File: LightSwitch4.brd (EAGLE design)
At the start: 40 x 44 mm, 9 parts, among them SW1 SWITCH-SPST-ILLUMINATED, SW2 SWITCH-SPST-ILLUMINATED, SW3 SWITCH-SPST-ILLUMINATED, SW4 SWITCH-SPST-ILLUMINATED

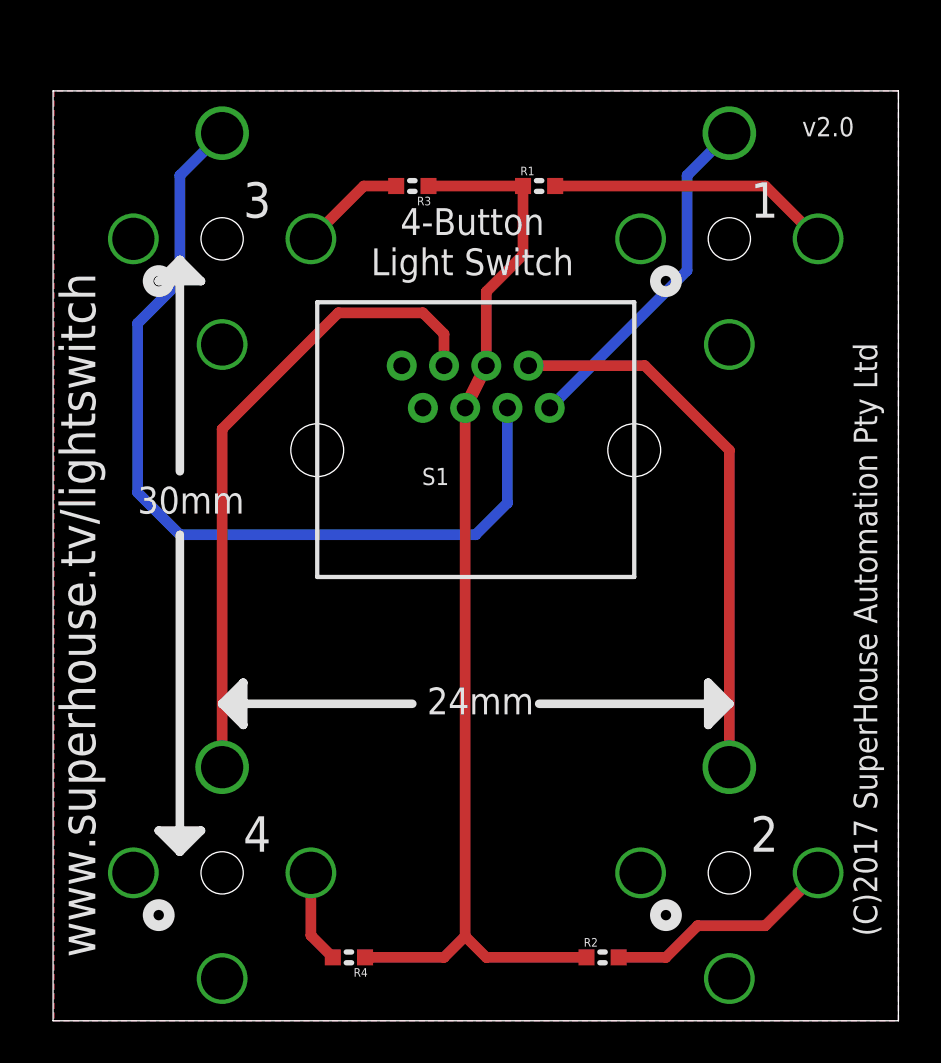
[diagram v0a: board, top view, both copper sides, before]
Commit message: Changed button footprint to slotted version for v2.1 release
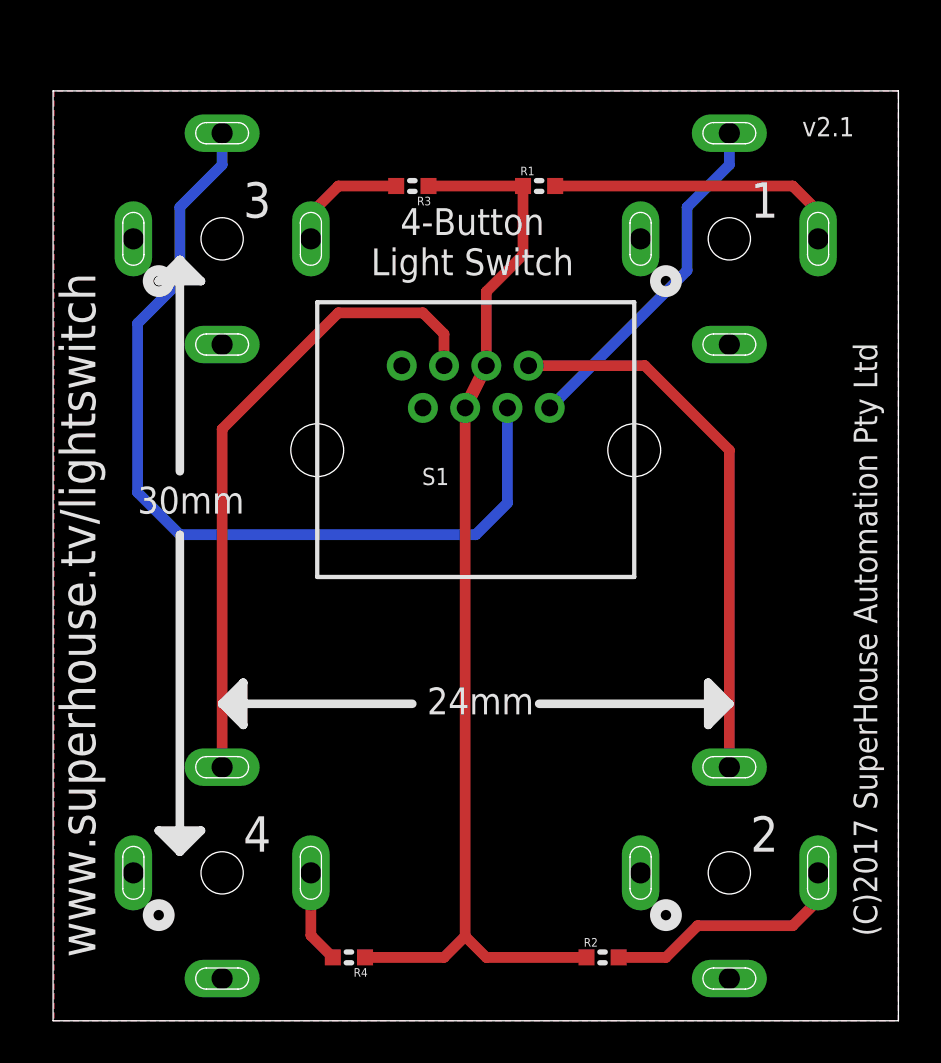
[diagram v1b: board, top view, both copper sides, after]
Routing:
- net N$1: track 11.1 -> 11.9 mm
- net N$6: track 13.5 -> 14.2 mm
- net N$7: track 5.07 -> 5.78 mm
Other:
- board text added: "v2.1"
- board text removed: "v2.0"
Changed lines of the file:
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@@
 <?xml version="1.0" encoding="utf-8"?>
 <!DOCTYPE eagle SYSTEM "eagle.dtd">
-<eagle version="8.3.2">
+<eagle version="8.7.0">
 <drawing>
 <settings>
-<setting alwaysvectorfont="yes"/>
+<setting alwaysvectorfont="no"/>
 <setting keepoldvectorfont="yes"/>
 <setting verticaltext="up"/>
@@
 <layer number="60" name="p_dimension" color="6" fill="0" visible="no" active="no"/>
 <layer number="61" name="pt_docu" color="7" fill="0" visible="no" active="no"/>
+<layer number="88" name="SimResults" color="9" fill="1" visible="no" active="no"/>
+<layer number="89" name="SimProbes" color="9" fill="1" visible="no" active="no"/>
 <layer number="90" name="Modules" color="7" fill="1" visible="no" active="no"/>
 <layer number="91" name="Nets" color="2" fill="1" visible="no" active="no"/>
@@
 <wire x1="40" y1="44" x2="40" y2="0" width="0" layer="20"/>
 <text x="39" y="4" size="1.1176" layer="21" font="vector" ratio="15" rot="R90">(C)2017 SuperHouse Automation Pty Ltd</text>
-<text x="35.4452" y="41.8486" size="0.9144" layer="21" font="vector" ratio="15">v2.0</text>
+<text x="35.4452" y="41.8486" size="0.9144" layer="21" font="vector" ratio="15">v2.1</text>
 <text x="19.8412" y="36.8646" size="1.27" layer="21" font="vector" ratio="15" align="center">4-Button
 Light Switch</text>
-<text x="2" y="3" size="1.6764" layer="21" ratio="15" rot="R90">www.superhouse.tv/lightswitch</text>
-<text x="33" y="38" size="1.6764" layer="21" ratio="15">1</text>
-<text x="33" y="8" size="1.6764" layer="21" ratio="15">2</text>
-<text x="9" y="38" size="1.6764" layer="21" ratio="15">3</text>
-<text x="9" y="8" size="1.6764" layer="21" ratio="15">4</text>
-<text x="17.7" y="14.5" size="1.27" layer="21" ratio="15">24mm</text>
+<text x="2" y="3" size="1.6764" layer="21" font="vector" ratio="15" rot="R90">www.superhouse.tv/lightswitch</text>
+<text x="33" y="38" size="1.6764" layer="21" font="vector" ratio="15">1</text>
+<text x="33" y="8" size="1.6764" layer="21" font="vector" ratio="15">2</text>
+<text x="9" y="38" size="1.6764" layer="21" font="vector" ratio="15">3</text>
+<text x="9" y="8" size="1.6764" layer="21" font="vector" ratio="15">4</text>
+<text x="17.7" y="14.5" size="1.27" layer="21" font="vector" ratio="15">24mm</text>
 <wire x1="17" y1="15" x2="8" y2="15" width="0.4064" layer="21"/>
 <wire x1="8" y1="15" x2="9" y2="16" width="0.4064" layer="21"/>
@@
 <wire x1="31" y1="16" x2="31" y2="14" width="0.4064" layer="21"/>
 <wire x1="31" y1="14" x2="32" y2="15" width="0.4064" layer="21"/>
-<text x="4" y="24" size="1.27" layer="21" ratio="15">30mm</text>
+<text x="4" y="24" size="1.27" layer="21" font="vector" ratio="15">30mm</text>
 <wire x1="6" y1="26" x2="6" y2="36" width="0.4064" layer="21"/>
 <wire x1="6" y1="36" x2="7" y2="35" width="0.4064" layer="21"/>
@@
 <param name="dpMaxLengthDifference" value="10mm"/>
 <param name="dpGapFactor" value="2.5"/>
-<param name="checkGrid" value="0"/>
 <param name="checkAngle" value="0"/>
 <param name="checkFont" value="1"/>
 <param name="checkRestrict" value="1"/>
+<param name="checkStop" value="0"/>
+<param name="checkValues" value="0"/>
 <param name="useDiameter" value="13"/>
 <param name="maxErrors" value="50"/>
@@
 <contactref element="SW1" pad="3"/>
 <wire x1="23.5" y1="29" x2="30" y2="35.5" width="0.508" layer="16"/>
-<wire x1="30" y1="40" x2="32" y2="42" width="0.508" layer="16"/>
-<wire x1="30" y1="35.5" x2="30" y2="40" width="0.508" layer="16"/>
+<wire x1="30" y1="35.5" x2="30" y2="38.5" width="0.508" layer="16"/>
+<wire x1="30" y1="38.5" x2="32" y2="40.5" width="0.508" layer="16"/>
+<wire x1="32" y1="40.5" x2="32" y2="42" width="0.508" layer="16"/>
 </signal>
 <signal name="N$5">
@@
 <wire x1="4" y1="25" x2="4" y2="33" width="0.508" layer="16"/>
 <wire x1="4" y1="33" x2="6" y2="35" width="0.508" layer="16"/>
-<wire x1="6" y1="35" x2="6" y2="40" width="0.508" layer="16"/>
-<wire x1="6" y1="40" x2="8" y2="42" width="0.508" layer="16"/>
+<wire x1="6" y1="35" x2="6" y2="38.5" width="0.508" layer="16"/>
+<wire x1="6" y1="38.5" x2="8" y2="40.5" width="0.508" layer="16"/>
+<wire x1="8" y1="40.5" x2="8" y2="42" width="0.508" layer="16"/>
 </signal>
 <signal name="N$3">
@@
 <contactref element="R2" pad="2"/>
 <wire x1="29" y1="3" x2="30.5" y2="4.5" width="0.508" layer="1"/>
-<wire x1="33.7" y1="4.5" x2="36.2" y2="7" width="0.508" layer="1"/>
 <wire x1="26.762" y1="3" x2="29" y2="3" width="0.508" layer="1"/>
-<wire x1="30.5" y1="4.5" x2="33.7" y2="4.5" width="0.508" layer="1"/>
+<wire x1="35" y1="4.5" x2="36.2" y2="5.7" width="0.508" layer="1"/>
+<wire x1="36.2" y1="5.7" x2="36.2" y2="7" width="0.508" layer="1"/>
+<wire x1="30.5" y1="4.5" x2="35" y2="4.5" width="0.508" layer="1"/>
 </signal>
 <signal name="N$6">
 <contactref element="SW1" pad="2"/>
 <contactref element="R1" pad="2"/>
-<wire x1="23.762" y1="39.5" x2="33.7" y2="39.5" width="0.508" layer="1"/>
-<wire x1="33.7" y1="39.5" x2="36.2" y2="37" width="0.508" layer="1"/>
+<wire x1="35" y1="39.5" x2="36.2" y2="38.3" width="0.508" layer="1"/>
+<wire x1="36.2" y1="38.3" x2="36.2" y2="37" width="0.508" layer="1"/>
+<wire x1="23.762" y1="39.5" x2="35" y2="39.5" width="0.508" layer="1"/>
 </signal>
 <signal name="N$7">
 <contactref element="SW3" pad="2"/>
 <contactref element="R3" pad="2"/>
-<wire x1="16.238" y1="39.5" x2="14.7" y2="39.5" width="0.508" layer="1"/>
-<wire x1="14.7" y1="39.5" x2="12.2" y2="37" width="0.508" layer="1"/>
+<wire x1="16.238" y1="39.5" x2="13.5" y2="39.5" width="0.508" layer="1"/>
+<wire x1="13.5" y1="39.5" x2="12.2" y2="38.2" width="0.508" layer="1"/>
+<wire x1="12.2" y1="38.2" x2="12.2" y2="37" width="0.508" layer="1"/>
 </signal>
 <signal name="N$8">
@@
 </signal>
 </signals>
-<errors>
-</errors>
 </board>
 </drawing>

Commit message: Updated RJ45 footprint for v2.2
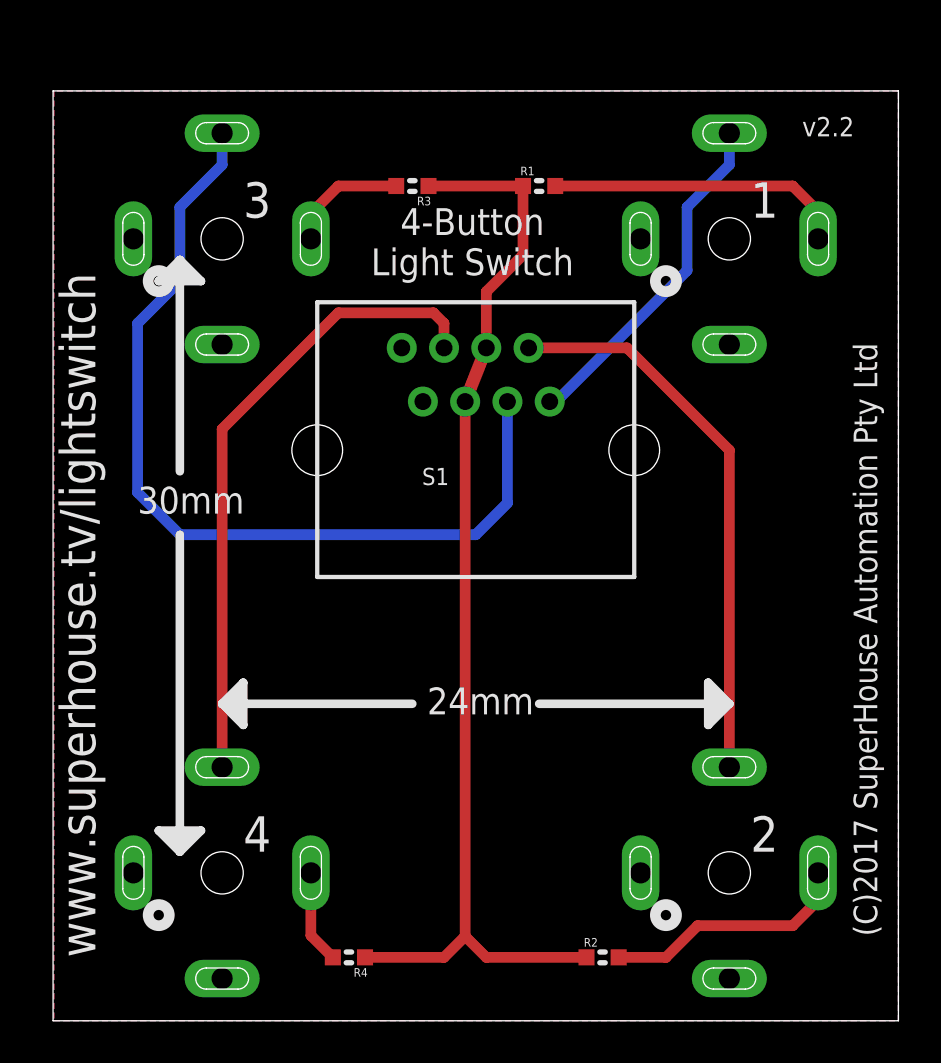
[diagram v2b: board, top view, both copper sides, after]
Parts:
- R1, R2, R3, R4: value 3K3 -> 4K7
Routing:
- net N$3: track 30.7 -> 30.1 mm
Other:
- board text added: "v2.2"
- board text removed: "v2.1"
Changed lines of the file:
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@@
 <wire x1="40" y1="44" x2="40" y2="0" width="0" layer="20"/>
 <text x="39" y="4" size="1.1176" layer="21" font="vector" ratio="15" rot="R90">(C)2017 SuperHouse Automation Pty Ltd</text>
-<text x="35.4452" y="41.8486" size="0.9144" layer="21" font="vector" ratio="15">v2.1</text>
+<text x="35.4452" y="41.8486" size="0.9144" layer="21" font="vector" ratio="15">v2.2</text>
 <text x="19.8412" y="36.8646" size="1.27" layer="21" font="vector" ratio="15" align="center">4-Button
 Light Switch</text>
@@
 <element name="SW3" library="freetronics-jon" package="SWITCH-SPST-ILLUMINATED" value="SWITCH-SPST-ILLUMINATED" x="8" y="37" rot="MR0"/>
 <element name="SW4" library="freetronics-jon" package="SWITCH-SPST-ILLUMINATED" value="SWITCH-SPST-ILLUMINATED" x="8" y="7" rot="MR0"/>
-<element name="R1" library="freetronics-jon" package="0603" value="3K3" x="23" y="39.5"/>
-<element name="R2" library="freetronics-jon" package="0603" value="3K3" x="26" y="3"/>
-<element name="R3" library="freetronics-jon" package="0603" value="3K3" x="17" y="39.5" rot="R180"/>
-<element name="R4" library="freetronics-jon" package="0603" value="3K3" x="14" y="3" rot="R180"/>
+<element name="R1" library="freetronics-jon" package="0603" value="4K7" x="23" y="39.5"/>
+<element name="R2" library="freetronics-jon" package="0603" value="4K7" x="26" y="3"/>
+<element name="R3" library="freetronics-jon" package="0603" value="4K7" x="17" y="39.5" rot="R180"/>
+<element name="R4" library="freetronics-jon" package="0603" value="4K7" x="14" y="3" rot="R180"/>
 </elements>
 <signals>
@@
 <contactref element="S1" pad="5"/>
 <contactref element="S1" pad="4"/>
-<wire x1="19.5" y1="29" x2="20.5" y2="31" width="0.6096" layer="1"/>
+<wire x1="19.5" y1="29.3" x2="20.5" y2="31.84" width="0.6096" layer="1"/>
 <contactref element="R4" pad="1"/>
 <contactref element="R3" pad="1"/>
@@
 <contactref element="R1" pad="1"/>
 <wire x1="22.238" y1="39.5" x2="17.762" y2="39.5" width="0.508" layer="1"/>
-<wire x1="20.5" y1="31" x2="20.5" y2="34.5" width="0.508" layer="1"/>
+<wire x1="20.5" y1="31.84" x2="20.5" y2="34.5" width="0.508" layer="1"/>
 <wire x1="22.238" y1="36.238" x2="22.238" y2="39.5" width="0.508" layer="1"/>
 <wire x1="20.5" y1="34.5" x2="22.238" y2="36.238" width="0.508" layer="1"/>
 <wire x1="19.5" y1="4" x2="20.5" y2="3" width="0.508" layer="1"/>
 <wire x1="20.5" y1="3" x2="25.238" y2="3" width="0.508" layer="1"/>
-<wire x1="19.5" y1="29" x2="19.5" y2="4" width="0.508" layer="1"/>
+<wire x1="19.5" y1="29.3" x2="19.5" y2="4" width="0.508" layer="1"/>
 <wire x1="14.762" y1="3" x2="18.5" y2="3" width="0.508" layer="1"/>
 <wire x1="18.5" y1="3" x2="19.5" y2="4" width="0.508" layer="1"/>
@@
 <contactref element="S1" pad="1"/>
 <contactref element="SW1" pad="3"/>
-<wire x1="23.5" y1="29" x2="30" y2="35.5" width="0.508" layer="16"/>
-<wire x1="30" y1="35.5" x2="30" y2="38.5" width="0.508" layer="16"/>
+<wire x1="30" y1="38.5" x2="30" y2="35.5" width="0.508" layer="16"/>
 <wire x1="30" y1="38.5" x2="32" y2="40.5" width="0.508" layer="16"/>
 <wire x1="32" y1="40.5" x2="32" y2="42" width="0.508" layer="16"/>
+<wire x1="30" y1="35.5" x2="23.8" y2="29.3" width="0.508" layer="16"/>
+<wire x1="23.8" y1="29.3" x2="23.5" y2="29.3" width="0.508" layer="16"/>
 </signal>
 <signal name="N$5">
@@
 <contactref element="SW2" pad="3"/>
 <wire x1="32" y1="12" x2="32" y2="27" width="0.508" layer="1"/>
-<wire x1="32" y1="27" x2="28" y2="31" width="0.508" layer="1"/>
-<wire x1="28" y1="31" x2="22.5" y2="31" width="0.508" layer="1"/>
+<wire x1="27.16" y1="31.84" x2="22.5" y2="31.84" width="0.508" layer="1"/>
+<wire x1="32" y1="27" x2="27.16" y2="31.84" width="0.508" layer="1"/>
 </signal>
 <signal name="N$2">
 <contactref element="S1" pad="3"/>
 <contactref element="SW3" pad="3"/>
-<wire x1="21.5" y1="29" x2="21.5" y2="24.5" width="0.508" layer="16"/>
+<wire x1="21.5" y1="29.3" x2="21.5" y2="24.5" width="0.508" layer="16"/>
 <wire x1="21.5" y1="24.5" x2="20" y2="23" width="0.508" layer="16"/>
 <wire x1="20" y1="23" x2="6" y2="23" width="0.508" layer="16"/>
@@
 <wire x1="8" y1="12" x2="8" y2="28" width="0.508" layer="1"/>
 <wire x1="8" y1="28" x2="13.5" y2="33.5" width="0.508" layer="1"/>
-<wire x1="13.5" y1="33.5" x2="17.5" y2="33.5" width="0.508" layer="1"/>
-<wire x1="17.5" y1="33.5" x2="18.5" y2="32.5" width="0.508" layer="1"/>
-<wire x1="18.5" y1="32.5" x2="18.5" y2="31" width="0.508" layer="1"/>
+<wire x1="18" y1="33.5" x2="18.5" y2="33" width="0.508" layer="1"/>
+<wire x1="18.5" y1="33" x2="18.5" y2="31.84" width="0.508" layer="1"/>
+<wire x1="13.5" y1="33.5" x2="18" y2="33.5" width="0.508" layer="1"/>
 </signal>
 <signal name="N$1">

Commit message: Release v2.2
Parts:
- S1: value RJ45 -> RJ45JC
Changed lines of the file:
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@@
 <?xml version="1.0" encoding="utf-8"?>
 <!DOCTYPE eagle SYSTEM "eagle.dtd">
-<eagle version="8.7.0">
+<eagle version="9.2.1">
 <drawing>
 <settings>
@@
 <param name="checkStop" value="0"/>
 <param name="checkValues" value="0"/>
+<param name="checkNames" value="1"/>
+<param name="checkWireStubs" value="1"/>
+<param name="checkPolygonWidth" value="0"/>
 <param name="useDiameter" value="13"/>
 <param name="maxErrors" value="50"/>
@@
 </autorouter>
 <elements>
-<element name="S1" library="freetronics-jon" package="RJ45" value="RJ45" x="20" y="27"/>
-<element name="SW1" library="freetronics-jon" package="SWITCH-SPST-ILLUMINATED" value="SWITCH-SPST-ILLUMINATED" x="32" y="37" rot="MR0"/>
-<element name="SW2" library="freetronics-jon" package="SWITCH-SPST-ILLUMINATED" value="SWITCH-SPST-ILLUMINATED" x="32" y="7" rot="MR0"/>
-<element name="SW3" library="freetronics-jon" package="SWITCH-SPST-ILLUMINATED" value="SWITCH-SPST-ILLUMINATED" x="8" y="37" rot="MR0"/>
-<element name="SW4" library="freetronics-jon" package="SWITCH-SPST-ILLUMINATED" value="SWITCH-SPST-ILLUMINATED" x="8" y="7" rot="MR0"/>
-<element name="R1" library="freetronics-jon" package="0603" value="4K7" x="23" y="39.5"/>
-<element name="R2" library="freetronics-jon" package="0603" value="4K7" x="26" y="3"/>
-<element name="R3" library="freetronics-jon" package="0603" value="4K7" x="17" y="39.5" rot="R180"/>
-<element name="R4" library="freetronics-jon" package="0603" value="4K7" x="14" y="3" rot="R180"/>
+<element name="S1" library="freetronics-jon" package="RJ45" value="RJ45JC" x="20" y="27" smashed="yes">
+<attribute name="NAME" x="17.46" y="25.35" size="0.8128" layer="25"/>
+<attribute name="VALUE" x="17.46" y="24.08" size="0.8128" layer="27"/>
+</element>
+<element name="SW1" library="freetronics-jon" package="SWITCH-SPST-ILLUMINATED" value="SWITCH-SPST-ILLUMINATED" x="32" y="37" smashed="yes" rot="MR0">
+<attribute name="NAME" x="34.49" y="38.62" size="1.016" layer="26" rot="MR0"/>
+<attribute name="VALUE" x="35.03" y="34.08" size="1.016" layer="28" rot="MR0"/>
+</element>
+<element name="SW2" library="freetronics-jon" package="SWITCH-SPST-ILLUMINATED" value="SWITCH-SPST-ILLUMINATED" x="32" y="7" smashed="yes" rot="MR0">
+<attribute name="NAME" x="34.49" y="8.62" size="1.016" layer="26" rot="MR0"/>
+<attribute name="VALUE" x="35.03" y="4.08" size="1.016" layer="28" rot="MR0"/>
+</element>
+<element name="SW3" library="freetronics-jon" package="SWITCH-SPST-ILLUMINATED" value="SWITCH-SPST-ILLUMINATED" x="8" y="37" smashed="yes" rot="MR0">
+<attribute name="NAME" x="10.49" y="38.62" size="1.016" layer="26" rot="MR0"/>
+<attribute name="VALUE" x="11.03" y="34.08" size="1.016" layer="28" rot="MR0"/>
+</element>
+<element name="SW4" library="freetronics-jon" package="SWITCH-SPST-ILLUMINATED" value="SWITCH-SPST-ILLUMINATED" x="8" y="7" smashed="yes" rot="MR0">
+<attribute name="NAME" x="10.49" y="8.62" size="1.016" layer="26" rot="MR0"/>
+<attribute name="VALUE" x="11.03" y="4.08" size="1.016" layer="28" rot="MR0"/>
+</element>
+<element name="R1" library="freetronics-jon" package="0603" value="4K7" x="23" y="39.5" smashed="yes">
+<attribute name="NAME" x="22.111" y="40.008" size="0.4064" layer="25" font="vector"/>
+<attribute name="VALUE" x="21.984" y="38.5348" size="0.4064" layer="27" font="vector"/>
+</element>
+<element name="R2" library="freetronics-jon" package="0603" value="4K7" x="26" y="3" smashed="yes">
+<attribute name="NAME" x="25.111" y="3.508" size="0.4064" layer="25" font="vector"/>
+<attribute name="VALUE" x="24.984" y="2.0348" size="0.4064" layer="27" font="vector"/>
+</element>
+<element name="R3" library="freetronics-jon" package="0603" value="4K7" x="17" y="39.5" smashed="yes" rot="R180">
+<attribute name="NAME" x="17.889" y="38.992" size="0.4064" layer="25" font="vector" rot="R180"/>
+<attribute name="VALUE" x="18.016" y="40.4652" size="0.4064" layer="27" font="vector" rot="R180"/>
+</element>
+<element name="R4" library="freetronics-jon" package="0603" value="4K7" x="14" y="3" smashed="yes" rot="R180">
+<attribute name="NAME" x="14.889" y="2.492" size="0.4064" layer="25" font="vector" rot="R180"/>
+<attribute name="VALUE" x="15.016" y="3.9652" size="0.4064" layer="27" font="vector" rot="R180"/>
+</element>
 </elements>
 <signals>
@@
 </signal>
 </signals>
+<mfgpreviewcolors>
+<mfgpreviewcolor name="soldermaskcolor" color="0xC8008000"/>
+<mfgpreviewcolor name="silkscreencolor" color="0xFFFEFEFE"/>
+<mfgpreviewcolor name="backgroundcolor" color="0xFF282828"/>
+<mfgpreviewcolor name="coppercolor" color="0xFFFFBF00"/>
+<mfgpreviewcolor name="substratecolor" color="0xFF786E46"/>
+</mfgpreviewcolors>
 </board>
 </drawing>
